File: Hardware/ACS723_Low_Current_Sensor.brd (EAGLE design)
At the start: 31.8 x 15.2 mm, 26 parts, among them U1 ACS723, U2 OPA344

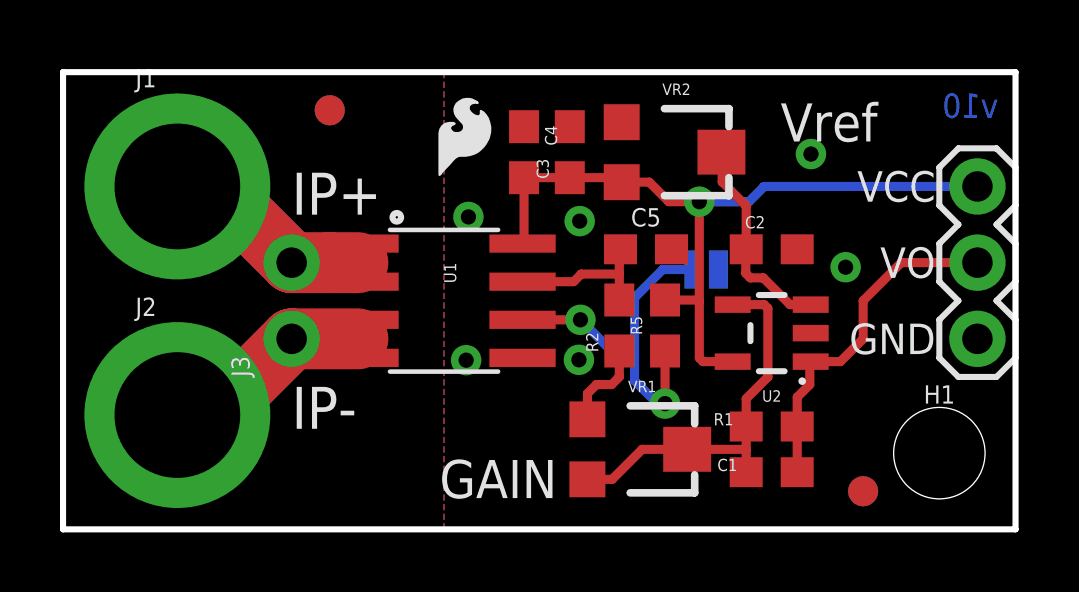
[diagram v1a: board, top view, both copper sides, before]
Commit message: v10 finalization
-moved some vias for better GND stitching
-slight silk adjustment
-changed value of opamp voltage split to allow for similiar spectrum measurment as the previous version. With an output of 220mV more per amp the values of the gain resistors needed to be adjusted to account for this difference
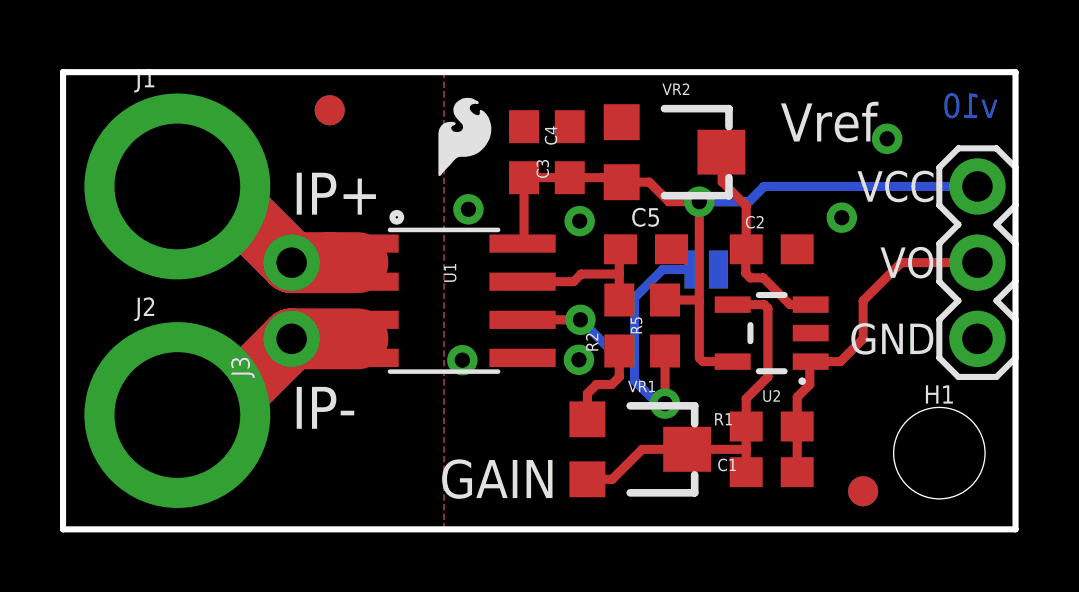
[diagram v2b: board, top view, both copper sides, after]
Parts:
- R1: value 47k -> 22k
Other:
- board text added: "20kHz-OPEN"
- board text added: "80kHz-CLOSED"
- board text added: "VOUT"
- board text removed: "20kHz"
- board text removed: "80kHz"
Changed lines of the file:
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@@
 <text x="31.1785" y="13.716" size="0.8128" layer="16" ratio="15" rot="MR0">v10</text>
 <text x="26.1874" y="11.938" size="1.016" layer="22" ratio="15" rot="MR180">VCC</text>
-<text x="27.1399" y="9.398" size="1.016" layer="22" ratio="15" rot="MR180">VO</text>
+<text x="25.2349" y="9.398" size="1.016" layer="22" ratio="15" rot="MR180">VOUT</text>
 <text x="26.2001" y="6.858" size="1.016" layer="22" ratio="15" rot="MR180">GND</text>
-<text x="18.9357" y="8.8265" size="0.8128" layer="22" font="vector" ratio="15" rot="MR0">80kHz</text>
-<text x="18.9357" y="7.6327" size="0.8128" layer="22" font="vector" ratio="15" rot="MR0">20kHz</text>
-<wire x1="20.2819" y1="8.636" x2="15.2654" y2="8.636" width="0.1524" layer="22"/>
+<text x="20.0787" y="8.8265" size="0.8128" layer="22" font="vector" ratio="15" rot="MR0">80kHz-CLOSED</text>
+<text x="20.0787" y="7.6327" size="0.8128" layer="22" font="vector" ratio="15" rot="MR0">20kHz-OPEN</text>
+<wire x1="20.2819" y1="8.636" x2="11.4554" y2="8.636" width="0.1524" layer="22"/>
 <text x="10.16" y="10.16" size="1.27" layer="22" ratio="15" rot="MR0">IP+</text>
 <text x="10.16" y="3.81" size="1.27" layer="22" ratio="15" rot="MR0">IP-</text>
@@
 <dimension x1="3.81" y1="11.43" x2="3.81" y2="3.81" x3="-2.54" y3="7.62" textsize="1.778" textratio="15" layer="47" dtype="horizontal" unit="inch"/>
 <text x="26.035" y="12.4714" size="1.016" layer="22" ratio="15" rot="MR0">Low Current Sensor</text>
-<wire x1="19.9517" y1="7.7343" x2="19.9517" y2="8.3693" width="0.127" layer="22"/>
-<wire x1="19.9517" y1="8.3693" x2="19.3167" y2="8.3693" width="0.127" layer="22"/>
-<wire x1="19.3167" y1="8.3693" x2="19.3167" y2="7.7343" width="0.127" layer="22"/>
-<wire x1="19.3167" y1="7.7343" x2="19.9517" y2="7.7343" width="0.127" layer="22"/>
-<wire x1="19.9517" y1="8.9027" x2="19.9517" y2="9.5377" width="0.127" layer="22"/>
-<wire x1="19.9517" y1="9.5377" x2="19.3167" y2="9.5377" width="0.127" layer="22"/>
-<wire x1="19.3167" y1="9.5377" x2="19.3167" y2="8.9027" width="0.127" layer="22"/>
-<wire x1="19.3167" y1="8.9027" x2="19.9517" y2="8.9027" width="0.127" layer="22"/>
-<rectangle x1="19.3548" y1="8.9408" x2="19.9136" y2="9.4996" layer="22" rot="R180"/>
+<dimension x1="29.21" y1="2.54" x2="0" y2="2.54" x3="14.605" y3="-2.54" textsize="1.778" textratio="15" layer="47" unit="inch"/>
 </plain>
 <attributes>
@@
 </autorouter>
 <elements>
-<element name="R1" library="SparkFun-Resistors" package="0603" value="47k" x="23.622" y="3.429" smashed="yes" rot="R180">
+<element name="R1" library="SparkFun-Resistors" package="0603" value="22k" x="23.622" y="3.429" smashed="yes" rot="R180">
 <attribute name="NAME" x="22.352" y="3.8735" size="0.4064" layer="25" rot="R180"/>
-<attribute name="VALUE" value="47k" x="24.892" y="3.8735" size="0.4064" layer="27" rot="R270"/>
-<attribute name="PROD_ID" value="RES-07871" x="23.622" y="3.429" size="1.778" layer="27" rot="R180" display="off"/>
+<attribute name="VALUE" value="22k" x="24.892" y="3.8735" size="0.4064" layer="27" rot="R270"/>
+<attribute name="PROD_ID" value="RES-07853" x="23.622" y="3.429" size="1.778" layer="27" rot="R180" display="off"/>
 </element>
 <element name="R2" library="SparkFun-Resistors" package="0603" value="1k" x="18.542" y="6.7945" smashed="yes" rot="R90">
@@
 <contactref element="C4" pad="1"/>
 <contactref element="U1" pad="5"/>
-<via x="13.4366" y="5.6388" extent="1-16" drill="0.508"/>
-<via x="26.0858" y="8.7376" extent="1-16" drill="0.508"/>
-<via x="13.5128" y="10.414" extent="1-16" drill="0.508"/>
+<via x="13.3096" y="5.6388" extent="1-16" drill="0.508"/>
+<via x="25.9588" y="10.3886" extent="1-16" drill="0.508"/>
+<via x="13.5128" y="10.668" extent="1-16" drill="0.508"/>
 <via x="17.1958" y="5.6515" extent="1-16" drill="0.508"/>
 <contactref element="VR2" pad="1"/>
 <contactref element="C3" pad="2"/>
 <contactref element="U2" pad="2"/>
-<via x="24.9301" y="12.5095" extent="1-16" drill="0.508"/>
+<via x="27.4701" y="13.0175" extent="1-16" drill="0.508"/>
 <contactref element="C5" pad="2"/>
 <via x="17.2212" y="10.2743" extent="1-16" drill="0.508"/>
